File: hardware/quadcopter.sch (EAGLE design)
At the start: 61 parts, among them J1 AVR_SPI_PRG_6NS, J2 HEADER-4POS-2X2-0.1IN-FEMALE-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, J3 HEADER-10POSTH-254X10, J4 HEADER-4POS-0.1IN-FEMALE-SMD-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, Q1 MOSFET-SI2302CDS-T1-E3CT-ND, Q2 MOSFET-SI2302CDS-T1-E3CT-ND, Q3 MOSFET-SI2302CDS-T1-E3CT-ND, Q4 MOSFET-SI2302CDS-T1-E3CT-ND, Q5 MOSFET-SI2302CDS-T1-E3CT-ND, Q6 MOSFET-SI2302CDS-T1-E3CT-ND, SW1 PUSHBUTTON_SMD-VERTICAL-1, U1 ATMEGA128RFA1, U2 LSM-IMU-497-18367-1-NDIMU, Y1 CRYSTAL5X3

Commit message: fixed power supply?
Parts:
- removed C16: 4.7uF, quadparts_prebuilt_2022:CAPACITOR-NP_SMD-2012-0805_CERAMIC-4.7UF
- added C13, C15: 1uF, quadparts_prebuilt_2022:CAPACITOR-NP_SMD-2012-0805_CERAMIC-1UF
- added C17: 47uF, quadparts_prebuilt_2022:CAPACITOR-POL_47UF-SMD-1206-TAJA
- C1, C2: value 4.7uF -> 1uF; device quadparts_prebuilt:CAPACITOR-NP_SMD-2012-0805_CERAMIC-4.7UF -> quadparts_prebuilt_2022:CAPACITOR-NP_SMD-2012-0805_CERAMIC-1UF
- C10, C11: device quadparts_prebuilt_2022:CAPACITOR-NP_SMD-2012-0805_CERAMIC-4.7UF -> quadparts_prebuilt_2022:CAPACITOR-NP_SMD-2012-0805_CERAMIC-0.1UF
- C14: value 47uF -> 1uF; device quadparts_prebuilt_2022:CAPACITOR-POL_47UF-SMD-1206-TAJA -> quadparts_prebuilt_2022:CAPACITOR-NP_SMD-2012-0805_CERAMIC-1UF
- C3: value 4.7uF -> 22pF; device quadparts_prebuilt_2022:CAPACITOR-NP_SMD-2012-0805_CERAMIC-4.7UF -> quadparts_prebuilt_2022:CAPACITOR-NP_SMD-2012-0805_CERAMIC-22PF
- C4, C5: value 4.7uF -> 12pF; device quadparts_prebuilt_2022:CAPACITOR-NP_SMD-2012-0805_CERAMIC-4.7UF -> quadparts_prebuilt_2022:CAPACITOR-NP_SMD-2012-0805_CERAMIC-12PF
- C6, C7: value 4.7uF -> 1uF; device quadparts_prebuilt_2022:CAPACITOR-NP_SMD-2012-0805_CERAMIC-4.7UF -> quadparts_prebuilt_2022:CAPACITOR-NP_SMD-2012-0805_CERAMIC-1UF
- C8: value 4.7uF -> 0.75pF; device quadparts_prebuilt_2022:CAPACITOR-NP_SMD-2012-0805_CERAMIC-4.7UF -> quadparts_prebuilt_2022:CAPACITOR-NP_SMD-2012-0805_CERAMIC-0.75PF
- C9: value 1uF -> 0.1uF; device quadparts_prebuilt_2022:CAPACITOR-NP_SMD-2012-0805_CERAMIC-4.7UF -> quadparts_prebuilt_2022:CAPACITOR-NP_SMD-2012-0805_CERAMIC-0.1UF
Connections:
- new net N$22: C14.1, REG.NC/FB
- net GND: now also C13.2, C14.2, C15.2, C17.-, C3.1; no longer C14.-, C16.2, C3.2
- net N$18: now also C13.1; no longer C14.+
- net N$5: now also C3.2; no longer C3.1
- net VBAT: now also C15.1, C17.+; no longer C16.1
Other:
- moved on the sheet: C3

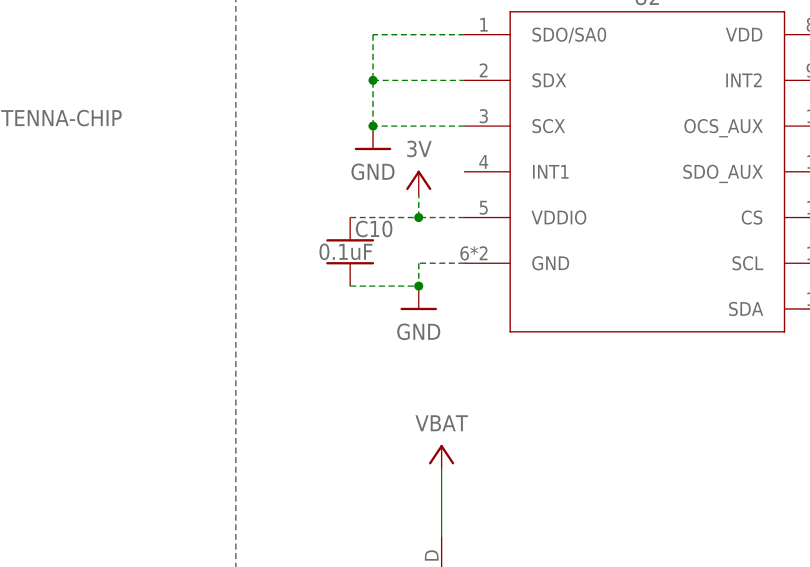
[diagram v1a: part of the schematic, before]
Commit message: fixed VDDIO error hopefully
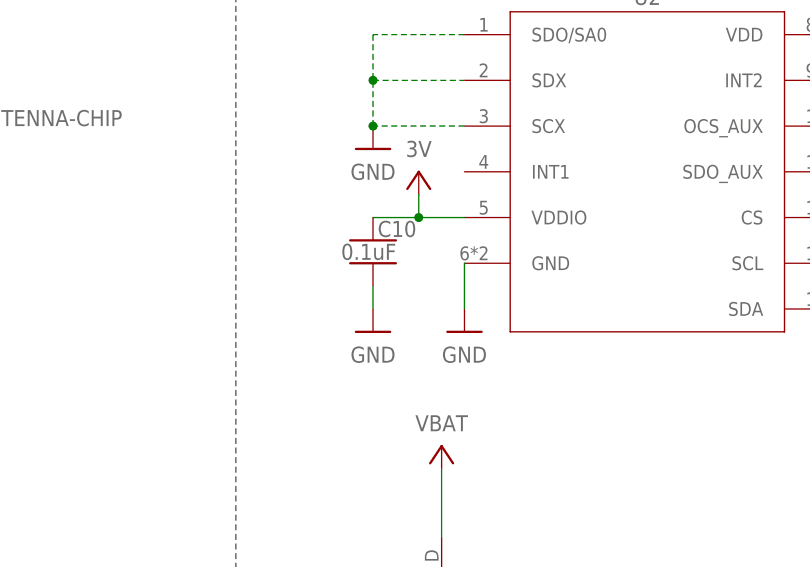
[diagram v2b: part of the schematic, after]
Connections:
- net 3V: now also C10.1, U2.VDDIO
- net VDDIO: no longer C10.1, U2.VDDIO
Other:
- moved on the sheet: C10
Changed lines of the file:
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@@
 <part name="GND16" library="quadparts_prebuilt_2022" deviceset="GND" device=""/>
 <part name="U2" library="custom.lbr" library_urn="urn:adsk.wipprod:fs.file:vf.FjMADskDQ2Se9fX1PD5xcw" deviceset="LSM-IMU" device="-497-18367-1-NDIMU"/>
-<part name="P+5" library="quadparts_prebuilt_2022" deviceset="3V" device=""/>
 <part name="P+6" library="quadparts_prebuilt_2022" deviceset="3V" device=""/>
-<part name="GND17" library="quadparts_prebuilt_2022" deviceset="GND" device=""/>
 <part name="GND18" library="quadparts_prebuilt_2022" deviceset="GND" device=""/>
 <part name="P+7" library="quadparts_prebuilt_2022" deviceset="3V" device=""/>
@@
 <part name="C8" library="quadparts_prebuilt_2022" deviceset="CAPACITOR-NP_" device="SMD-2012-0805_CERAMIC-0.75PF" value="0.75pF"/>
 <part name="C9" library="quadparts_prebuilt_2022" deviceset="CAPACITOR-NP_" device="SMD-2012-0805_CERAMIC-0.1UF" value="0.1uF"/>
-<part name="C10" library="quadparts_prebuilt_2022" deviceset="CAPACITOR-NP_" device="SMD-2012-0805_CERAMIC-0.1UF" value="0.1uF"/>
 <part name="C11" library="quadparts_prebuilt_2022" deviceset="CAPACITOR-NP_" device="SMD-2012-0805_CERAMIC-0.1UF" value="0.1uF"/>
 <part name="C15" library="quadparts_prebuilt_2022" deviceset="CAPACITOR-NP_" device="SMD-2012-0805_CERAMIC-1UF" value="1uF"/>
@@
 <part name="C14" library="quadparts_prebuilt_2022" deviceset="CAPACITOR-NP_" device="SMD-2012-0805_CERAMIC-1UF" value="1uF"/>
 <part name="C17" library="quadparts_prebuilt_2022" deviceset="CAPACITOR-POL_" device="47UF-SMD-1206-TAJA" package3d_urn="urn:adsk.eagle:package:11793387/1" value="47uF"/>
+<part name="P+5" library="quadparts_prebuilt_2022" deviceset="3V" device=""/>
+<part name="C10" library="quadparts_prebuilt_2022" deviceset="CAPACITOR-NP_" device="SMD-2012-0805_CERAMIC-0.1UF" value="0.1uF"/>
+<part name="GND17" library="quadparts_prebuilt_2022" deviceset="GND" device=""/>
+<part name="GND48" library="quadparts_prebuilt_2022" deviceset="GND" device=""/>
 </parts>
 <sheets>
@@
 <attribute name="NAME" x="261.62" y="177.8" size="1.778" layer="95" align="top-center"/>
 </instance>
-<instance part="P+5" gate="G$1" x="236.22" y="157.48" smashed="yes">
-<attribute name="VALUE" x="236.22" y="160.02" size="1.778" layer="96" rot="R180" align="center"/>
-</instance>
 <instance part="P+6" gate="G$1" x="287.02" y="177.8" smashed="yes">
 <attribute name="VALUE" x="287.02" y="180.34" size="1.778" layer="96" rot="R180" align="center"/>
-</instance>
-<instance part="GND17" gate="1" x="236.22" y="142.24" smashed="yes">
-<attribute name="VALUE" x="236.22" y="139.7" size="1.778" layer="96" align="center"/>
 </instance>
 <instance part="GND18" gate="1" x="231.14" y="160.02" smashed="yes">
@@
 <attribute name="NAME" x="333.248" y="211.201" size="1.778" layer="95"/>
 </instance>
-<instance part="C10" gate="G$1" x="228.6" y="149.86" smashed="yes">
-<attribute name="VALUE" x="225.044" y="147.701" size="1.778" layer="96"/>
-<attribute name="NAME" x="229.108" y="150.241" size="1.778" layer="95"/>
-</instance>
 <instance part="C11" gate="G$1" x="297.18" y="170.18" smashed="yes">
 <attribute name="VALUE" x="293.624" y="168.021" size="1.778" layer="96"/>
@@
 <attribute name="VALUE" x="212.344" y="33.401" size="1.778" layer="96"/>
 <attribute name="NAME" x="216.154" y="35.941" size="1.778" layer="95"/>
+</instance>
+<instance part="P+5" gate="G$1" x="236.22" y="157.48" smashed="yes">
+<attribute name="VALUE" x="236.22" y="160.02" size="1.778" layer="96" rot="R180" align="center"/>
+</instance>
+<instance part="C10" gate="G$1" x="231.14" y="149.86" smashed="yes">
+<attribute name="VALUE" x="227.584" y="147.701" size="1.778" layer="96"/>
+<attribute name="NAME" x="231.648" y="150.241" size="1.778" layer="95"/>
+</instance>
+<instance part="GND17" gate="1" x="231.14" y="139.7" smashed="yes">
+<attribute name="VALUE" x="231.14" y="137.16" size="1.778" layer="96" align="center"/>
+</instance>
+<instance part="GND48" gate="1" x="241.3" y="139.7" smashed="yes">
+<attribute name="VALUE" x="241.3" y="137.16" size="1.778" layer="96" align="center"/>
 </instance>
 </instances>
@@
 </segment>
 <segment>
-<wire x1="228.6" y1="144.78" x2="236.22" y2="144.78" width="0.1524" layer="91" style="longdash"/>
-<pinref part="GND17" gate="1" pin="GND"/>
-<pinref part="U2" gate="G$1" pin="GND"/>
-<wire x1="241.3" y1="147.32" x2="236.22" y2="147.32" width="0.1524" layer="91" style="longdash"/>
-<wire x1="236.22" y1="147.32" x2="236.22" y2="144.78" width="0.1524" layer="91" style="longdash"/>
-<junction x="236.22" y="144.78"/>
-<pinref part="C10" gate="G$1" pin="2"/>
-</segment>
-<segment>
 <pinref part="R6" gate="G$1" pin="2"/>
 <wire x1="17.78" y1="0" x2="10.16" y2="0" width="0.1524" layer="91"/>
@@
 <pinref part="C14" gate="G$1" pin="2"/>
 </segment>
+<segment>
+<pinref part="C10" gate="G$1" pin="2"/>
+<wire x1="231.14" y1="144.78" x2="231.14" y2="142.24" width="0.1524" layer="91"/>
+<pinref part="GND17" gate="1" pin="GND"/>
+</segment>
+<segment>
+<pinref part="GND48" gate="1" pin="GND"/>
+<wire x1="241.3" y1="142.24" x2="241.3" y2="147.32" width="0.1524" layer="91"/>
+<pinref part="U2" gate="G$1" pin="GND"/>
+</segment>
 </net>
 <net name="PG1" class="0">
@@
 <wire x1="340.36" y1="180.34" x2="347.98" y2="180.34" width="0.1524" layer="91"/>
 <pinref part="J3" gate="G$1" pin="10"/>
+</segment>
+<segment>
+<pinref part="U2" gate="G$1" pin="VDDIO"/>
+<wire x1="241.3" y1="152.4" x2="236.22" y2="152.4" width="0.1524" layer="91"/>
+<wire x1="236.22" y1="152.4" x2="236.22" y2="154.94" width="0.1524" layer="91"/>
+<pinref part="P+5" gate="G$1" pin="3V"/>
+<wire x1="236.22" y1="152.4" x2="231.14" y2="152.4" width="0.1524" layer="91"/>
+<junction x="236.22" y="152.4"/>
+<pinref part="C10" gate="G$1" pin="1"/>
 </segment>
 </net>
@@
 <net name="VDDIO" class="0">
 <segment>
-<pinref part="U2" gate="G$1" pin="VDDIO"/>
-<wire x1="241.3" y1="152.4" x2="236.22" y2="152.4" width="0.1524" layer="91" style="longdash"/>
-<wire x1="236.22" y1="152.4" x2="236.22" y2="154.94" width="0.1524" layer="91" style="longdash"/>
-<pinref part="P+5" gate="G$1" pin="3V"/>
-<wire x1="228.6" y1="152.4" x2="236.22" y2="152.4" width="0.1524" layer="91" style="longdash"/>
-<junction x="236.22" y="152.4"/>
-<pinref part="C10" gate="G$1" pin="1"/>
-</segment>
-<segment>
 <pinref part="R4" gate="G$1" pin="1"/>

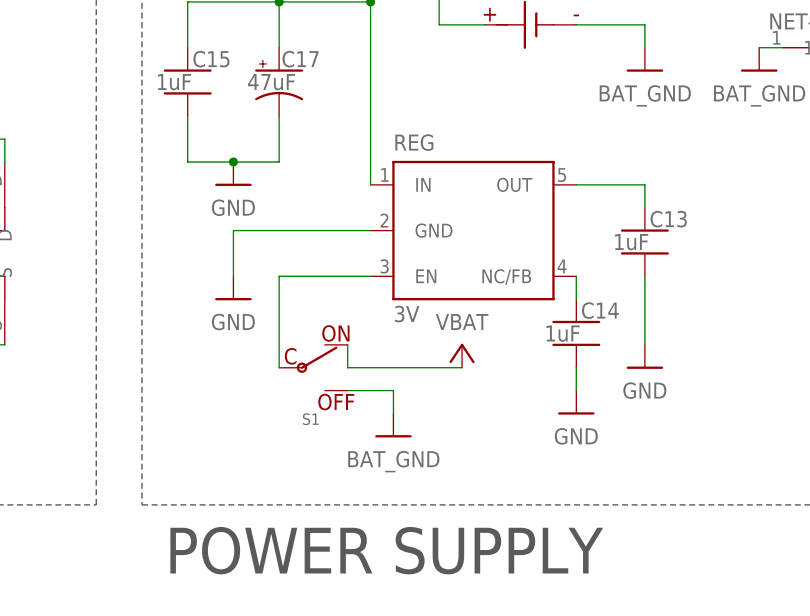
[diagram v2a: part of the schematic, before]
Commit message: attempt to fix power supply
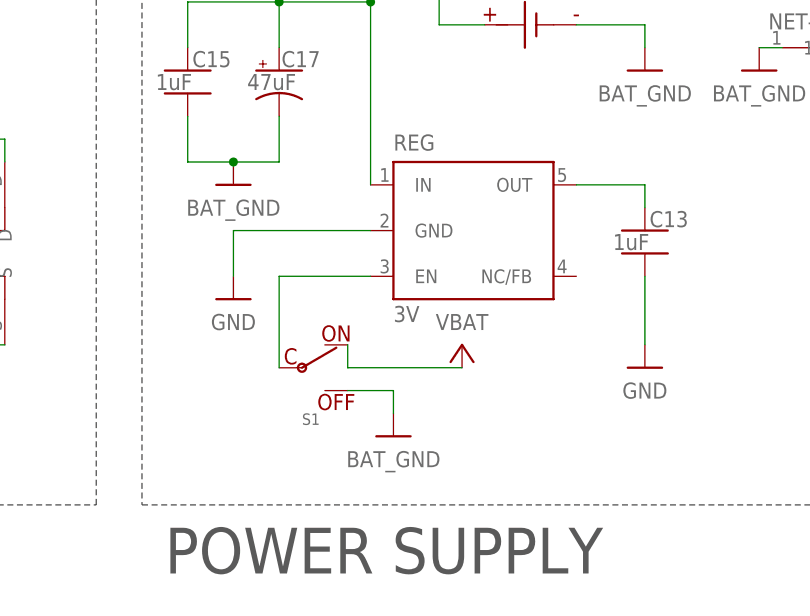
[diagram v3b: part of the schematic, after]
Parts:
- removed C14: 1uF, quadparts_prebuilt_2022:CAPACITOR-NP_SMD-2012-0805_CERAMIC-1UF
- B2: value BATTERY-SCREW-TERMINAL-SMD -> BATTERY-SCREW-TERMINAL-MINI-SMD; device quadparts_prebuilt_2022:BATTERY-SCREW-TERMINAL-SMD -> quadparts_prebuilt_2022:BATTERY-SCREW-TERMINAL-MINI-SMD
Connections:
- removed net N$22: C14.1, REG.NC/FB
- net BAT_GND: now also C15.2, C17.-
- net GND: no longer C14.2, C15.2, C17.-
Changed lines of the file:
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@@
 <part name="Q4" library="custom.lbr" library_urn="urn:adsk.wipprod:fs.file:vf.FjMADskDQ2Se9fX1PD5xcw" deviceset="MOSFET" device="-SI2302CDS-T1-E3CT-ND"/>
 <part name="C12" library="quadparts_prebuilt_2022" deviceset="CAPACITOR-POL_" device="47UF-SMD-1206-TAJA" package3d_urn="urn:adsk.eagle:package:11793387/1" value="47uF"/>
-<part name="B2" library="quadparts_prebuilt_2022" deviceset="BATTERY" device="-SCREW-TERMINAL-SMD"/>
 <part name="REG" library="quadparts_prebuilt_2022" deviceset="TPS73633-DBVT" device="3V" value="3V"/>
 <part name="P+12" library="quadparts_prebuilt_2022" deviceset="VBAT" device=""/>
 <part name="S1" library="quadparts_prebuilt_2022" deviceset="POWER-SWITCH-MFS201N-9-Z" device="-SMD-EDGE"/>
 <part name="GND32" library="quadparts_prebuilt_2022" deviceset="BAT_GND" device=""/>
-<part name="GND33" library="quadparts_prebuilt_2022" deviceset="GND" device=""/>
 <part name="GND35" library="quadparts_prebuilt_2022" deviceset="GND" device=""/>
 <part name="GND36" library="quadparts_prebuilt_2022" deviceset="GND" device=""/>
@@
 <part name="C15" library="quadparts_prebuilt_2022" deviceset="CAPACITOR-NP_" device="SMD-2012-0805_CERAMIC-1UF" value="1uF"/>
 <part name="C13" library="quadparts_prebuilt_2022" deviceset="CAPACITOR-NP_" device="SMD-2012-0805_CERAMIC-1UF" value="1uF"/>
-<part name="GND47" library="quadparts_prebuilt_2022" deviceset="GND" device=""/>
-<part name="C14" library="quadparts_prebuilt_2022" deviceset="CAPACITOR-NP_" device="SMD-2012-0805_CERAMIC-1UF" value="1uF"/>
 <part name="C17" library="quadparts_prebuilt_2022" deviceset="CAPACITOR-POL_" device="47UF-SMD-1206-TAJA" package3d_urn="urn:adsk.eagle:package:11793387/1" value="47uF"/>
 <part name="P+5" library="quadparts_prebuilt_2022" deviceset="3V" device=""/>
@@
 <part name="GND17" library="quadparts_prebuilt_2022" deviceset="GND" device=""/>
 <part name="GND48" library="quadparts_prebuilt_2022" deviceset="GND" device=""/>
+<part name="B2" library="quadparts_prebuilt_2022" deviceset="BATTERY" device="-SCREW-TERMINAL-MINI-SMD"/>
+<part name="GND33" library="quadparts_prebuilt_2022" deviceset="BAT_GND" device=""/>
 </parts>
 <sheets>
@@
 <attribute name="NAME" x="-4.826" y="30.861" size="1.778" layer="95"/>
 </instance>
-<instance part="B2" gate="G$1" x="243.84" y="40.64" smashed="yes">
-<attribute name="NAME" x="242.57" y="45.72" size="1.778" layer="95" font="vector" align="center"/>
-</instance>
 <instance part="REG" gate="G$1" x="228.6" y="10.16" smashed="yes">
 <attribute name="VALUE" x="228.6" y="7.62" size="1.778" layer="96"/>
@@
 <attribute name="VALUE" x="228.6" y="-7.62" size="1.778" layer="96" align="center"/>
 </instance>
-<instance part="GND33" gate="1" x="210.82" y="22.86" smashed="yes">
-<attribute name="VALUE" x="210.82" y="20.32" size="1.778" layer="96" align="center"/>
-</instance>
 <instance part="GND35" gate="1" x="256.54" y="2.54" smashed="yes">
 <attribute name="VALUE" x="256.54" y="0" size="1.778" layer="96" align="center"/>
@@
 <attribute name="NAME" x="257.048" y="18.161" size="1.778" layer="95"/>
 </instance>
-<instance part="GND47" gate="1" x="248.92" y="-2.54" smashed="yes">
-<attribute name="VALUE" x="248.92" y="-5.08" size="1.778" layer="96" align="center"/>
-</instance>
-<instance part="C14" gate="G$1" x="248.92" y="7.62" smashed="yes">
-<attribute name="VALUE" x="245.364" y="5.461" size="1.778" layer="96"/>
-<attribute name="NAME" x="249.428" y="8.001" size="1.778" layer="95"/>
-</instance>
 <instance part="C17" gate="G$1" x="215.9" y="35.56" smashed="yes">
 <attribute name="VALUE" x="212.344" y="33.401" size="1.778" layer="96"/>
@@
 <instance part="GND48" gate="1" x="241.3" y="139.7" smashed="yes">
 <attribute name="VALUE" x="241.3" y="137.16" size="1.778" layer="96" align="center"/>
+</instance>
+<instance part="B2" gate="G$1" x="243.84" y="40.64" smashed="yes">
+<attribute name="NAME" x="242.57" y="45.72" size="1.778" layer="95" font="vector" align="center"/>
+</instance>
+<instance part="GND33" gate="1" x="210.82" y="22.86" smashed="yes">
+<attribute name="VALUE" x="210.82" y="20.32" size="1.778" layer="96" align="center"/>
 </instance>
 </instances>
@@
 </segment>
 <segment>
-<pinref part="GND33" gate="1" pin="GND"/>
-<wire x1="205.74" y1="30.48" x2="205.74" y2="25.4" width="0.1524" layer="91"/>
-<wire x1="205.74" y1="25.4" x2="210.82" y2="25.4" width="0.1524" layer="91"/>
-<pinref part="C15" gate="G$1" pin="2"/>
-<wire x1="215.9" y1="30.48" x2="215.9" y2="25.4" width="0.1524" layer="91"/>
-<wire x1="215.9" y1="25.4" x2="210.82" y2="25.4" width="0.1524" layer="91"/>
-<pinref part="C17" gate="G$1" pin="-"/>
-<junction x="210.82" y="25.4"/>
-</segment>
-<segment>
 <wire x1="297.18" y1="165.1" x2="299.72" y2="165.1" width="0.1524" layer="91" style="longdash"/>
 <pinref part="GND19" gate="1" pin="GND"/>
 <pinref part="C11" gate="G$1" pin="2"/>
-</segment>
-<segment>
-<wire x1="248.92" y1="2.54" x2="248.92" y2="0" width="0.1524" layer="91"/>
-<pinref part="GND47" gate="1" pin="GND"/>
-<pinref part="C14" gate="G$1" pin="2"/>
 </segment>
 <segment>
@@
 </segment>
 <segment>
-<pinref part="B2" gate="G$1" pin="N"/>
 <wire x1="248.92" y1="40.64" x2="256.54" y2="40.64" width="0.1524" layer="91"/>
 <wire x1="256.54" y1="40.64" x2="256.54" y2="38.1" width="0.1524" layer="91"/>
 <pinref part="GND34" gate="1" pin="BAT_GND"/>
+<pinref part="B2" gate="G$1" pin="N"/>
 </segment>
 <segment>
@@
 <wire x1="337.82" y1="96.52" x2="337.82" y2="88.9" width="0.1524" layer="91"/>
 <pinref part="GND45" gate="1" pin="BAT_GND"/>
+</segment>
+<segment>
+<wire x1="205.74" y1="30.48" x2="205.74" y2="25.4" width="0.1524" layer="91"/>
+<pinref part="C15" gate="G$1" pin="2"/>
+<wire x1="215.9" y1="30.48" x2="215.9" y2="25.4" width="0.1524" layer="91"/>
+<wire x1="215.9" y1="25.4" x2="210.82" y2="25.4" width="0.1524" layer="91"/>
+<pinref part="C17" gate="G$1" pin="-"/>
+<pinref part="GND33" gate="1" pin="BAT_GND"/>
+<wire x1="210.82" y1="25.4" x2="205.74" y2="25.4" width="0.1524" layer="91"/>
+<junction x="210.82" y="25.4"/>
 </segment>
 </net>
@@
 </segment>
 </net>
-<net name="N$22" class="0">
-<segment>
-<pinref part="REG" gate="G$1" pin="NC/FB"/>
-<wire x1="248.92" y1="12.7" x2="248.92" y2="10.16" width="0.1524" layer="91"/>
-<pinref part="C14" gate="G$1" pin="1"/>
-</segment>
-</net>
